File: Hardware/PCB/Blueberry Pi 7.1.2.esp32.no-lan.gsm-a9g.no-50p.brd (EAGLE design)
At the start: 80.7 x 60.9 mm, 231 parts, among them J2 AUDIO_JACK_SMD, J3 USB-A-FEMALE, Q1 24Mhz, Q2 32kHz, U1 MICROSIM, U2 W25Q32FV, U3 AP3031KTR-G1, U4 ESP-WROOM-32, U5 W25Q40BVSS, X1 FH12-50S-0.5SH, X2 53047-02

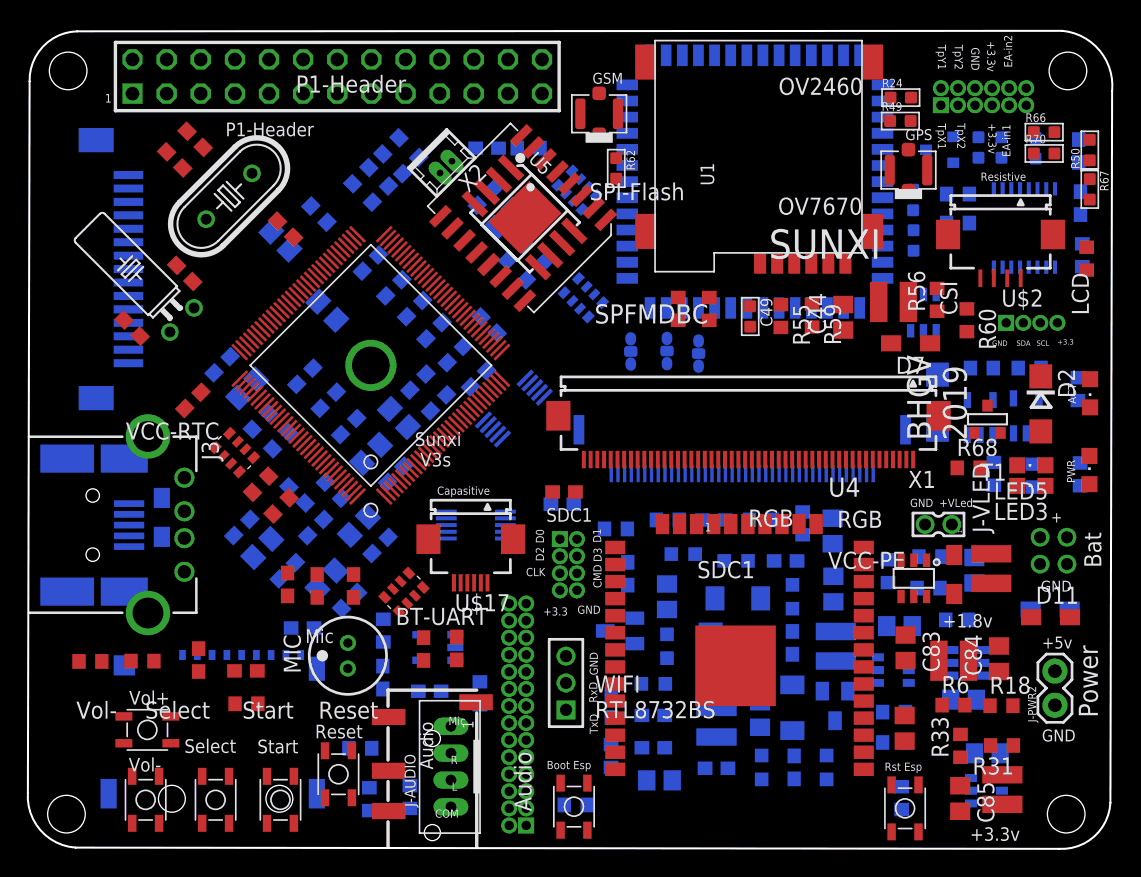
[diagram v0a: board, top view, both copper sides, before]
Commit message: better connected A9G module. added 'no-50pin lcd' schematic easier for router and with headers for the rest of A9G pins
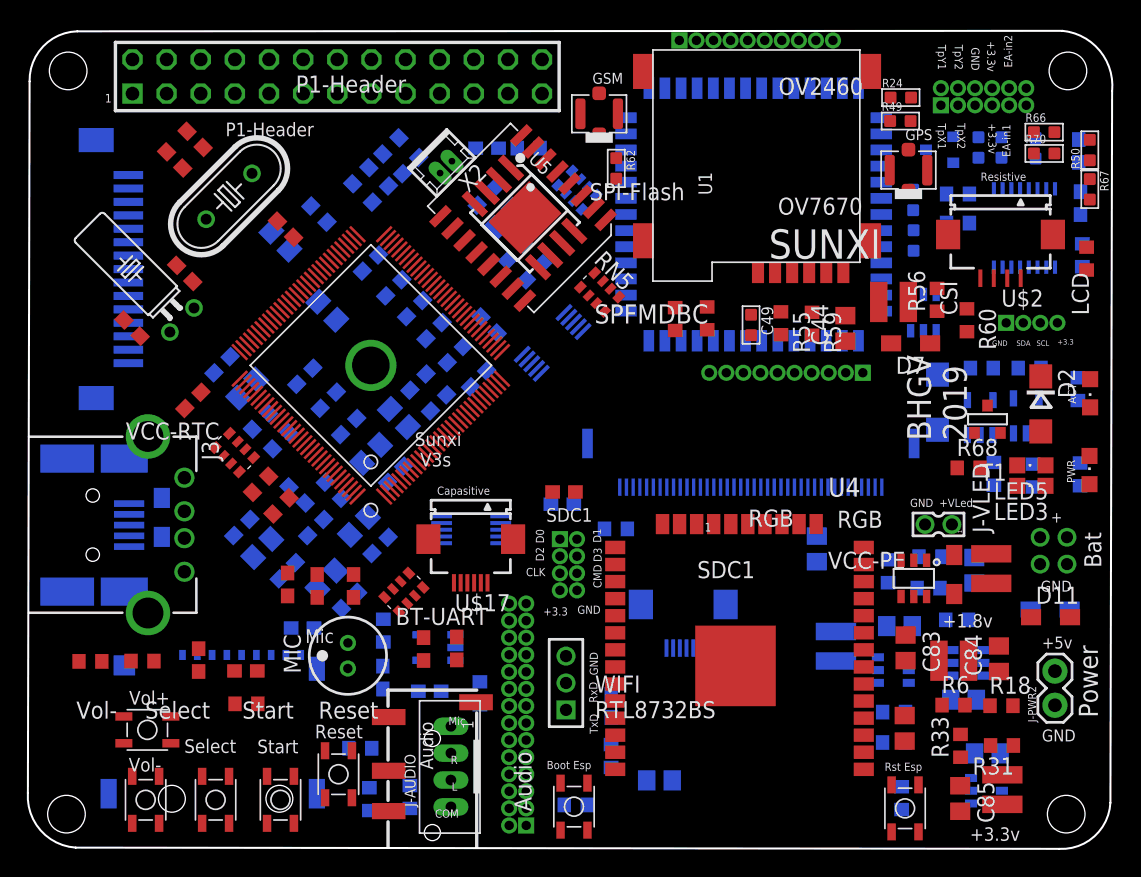
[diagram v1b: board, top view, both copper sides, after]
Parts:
- removed C31, C6: 22uF/6.3V, rcl:C0805
- removed C32, C33, C35, C4, C40, C41, C42, C43: 100nF, rcl:C0603
- removed C5: 10uF/16V, rcl:C0805
- removed D3, D4: BAT54S, semicon-smd-ipc:SOT23C(BAT54S)
- removed D5: 1N5819/SS14, gogo:MINI-MELF
- removed JMP1, JMP2, JMP3: 0R-JUMPC, jump-0r-smd:C0R-JMP
- removed L3: 47µH, induct-CD:CD32
- removed R10, R7: 10k, rcl:R0603
- removed R19, R40, R42: 51k/1%, rcl:R0603_5MIL
- removed R34, R37, R41: 1k/1%, rcl:R0603_5MIL
- removed R35: 20k, rcl:R0603_5MIL
- removed R9: 30k, rcl:R0603
- removed U3: AP3031KTR-G1, OLIMEX_IC:SOT23-6
- removed X1: FH12-50S-0.5SH, con-hirose:FH12-50S-0.5SH
- removed Z1: BZV55C6V8, gogo:MINI-MELF
- removed Z2: BZV55C16, gogo:MINI-MELF
- added DBG-COM1, DBG-COM2: HDR-1.27MM-110, headers-1.27:HDR-1.27MM-1*10
- added U$21: FH12-06S-0.5S, con-hirose:FH12-6S-0.5SH
- moved U$19 5.68 mm to (50.5, 38.1), turned to 135 degrees
- moved U6 2.45 mm to (65.4, 47.6)
- moved C73 1.78 mm to (70.1, 22.7)
- moved RN5 1.28 mm to (54.0, 41.8), flipped to the top, turned to 315 degrees
- moved J-LCD-FFC 1.20 mm to (65.2, 30.5)
- moved C44 0.84 mm to (72.3, 39.1)
- moved R44 0.79 mm to (59.6, 39.8)
- moved R45 0.72 mm to (62.0, 39.9)
- moved U1 0.72 mm to (73.3, 44.1)
- moved C49 0.64 mm to (65.2, 39.4)
- moved R59 0.60 mm to (69.8, 39.5)
- moved R55 0.54 mm to (67.5, 39.5)
- moved U$24 0.49 mm to (44.4, 24.2)
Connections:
- removed net -7V: C43.1, R41.1, R42.2, X1.42, Z1.2
- removed net 10.4V: C32.1, C5.1, D4.1, D5.1, R19.2, R35.2, U3.5, X1.43
- removed net 16V: C40.1, R37.1, R40.2, R9.1, X1.41, Z2.1
- removed net L/R: JMP1.2, X1.39
- removed net N$123: C33.1, C41.2, D5.2, L3.P$2, U3.1
- removed net N$126: R19.1, R34.1, U3.3
- removed net N$17: C4.1, R10.2, X1.44
- removed net N$24: JMP3.2, X1.47
- removed net N$25: C33.2, D4.3
- removed net N$27: C35.1, D4.2, R37.2
- removed net N$34: C42.1, D3.1, R41.2
- removed net N$37: C41.1, D3.3
- removed net U/D: JMP2.2, X1.40
- removed net VCOM: R7.1, R9.2, X1.46, X1.6
- new net A9G_HST_RXD: DBG-COM1.P$1, U6.38
- new net A9G_HST_TXD: DBG-COM1.P$2, U6.37
- new net A9G_IO26: DBG-COM2.P$7, U6.25
- new net A9G_IO27: DBG-COM2.P$8, U6.26
- new net A9G_IO28: DBG-COM2.P$9, U6.30
- new net A9G_IO29: DBG-COM1.P$8, U6.24
- new net A9G_IO30: DBG-COM2.P$10, U6.31
- new net A9G_LCD_CS: DBG-COM1.P$7, U6.19
- new net A9G_LCD_DIO: DBG-COM1.P$5, U6.21
- new net A9G_LCD_RST: DBG-COM1.P$6, U6.20
- new net A9G_LCD_SCK: DBG-COM1.P$3, U6.23
- new net A9G_LCD_SDC: DBG-COM1.P$4, U6.22
- new net A9G_SD_CLK: DBG-COM2.P$6, U6.8
- new net A9G_SD_CMD: DBG-COM2.P$5, U6.7
- new net A9G_SD_D0: DBG-COM2.P$4, U6.6
- new net A9G_SD_D1: DBG-COM2.P$3, U6.5
- new net A9G_SD_D2: DBG-COM2.P$2, U6.4
- new net A9G_SD_D3: DBG-COM2.P$1, U6.3
- new net N$85: J-LCD-FFC.1
- net !RESET: now also U$21.6
- net +3V3: now also DBG-COM1.P$9, U$21.5; no longer JMP1.3, JMP2.3, JMP3.1, R10.1, X1.7, X1.8
- net +5V: no longer C31.2, C6.2, L3.P$1, U3.4, U3.6
- net CSI_D0/LCD_D2: no longer X1.17
- net CSI_D1/LCD_D3: no longer X1.16
- net CSI_D10/LCD_D14: no longer X1.21
- net CSI_D11/LCD_D15: no longer X1.20
- net CSI_D12/LCD_D18: no longer X1.33
- net CSI_D2/LCD_D4: no longer X1.15
- net CSI_D3/LCD_D5: no longer X1.14
- net CSI_D4/LCD_D6: no longer X1.13
- net CSI_D5/LCD_D7: no longer X1.12
- net CSI_D6/LCD_D10: no longer X1.25
- net CSI_D7/LCD_D11: no longer X1.24
- net CSI_D8/LCD_D12: no longer X1.23
- net CSI_D9/LCD_D13: no longer X1.22
- net CSI_HSYNC/LCD_HSYNC: no longer X1.11
- net CSI_MCLK/LCD_DE: no longer X1.9
- net CSI_PCLK/LCD_CLK: no longer X1.37
- net CSI_VSYNC/LCD_VSYNC: no longer X1.10
- net GND: now also DBG-COM1.P$10, U$21.4; no longer C31.1, C32.2, C35.2, C4.2, C40.2, C42.2, C43.2, C5.2, C6.1, D3.2, JMP1.1, JMP2.1, JMP3.3, R34.2, R35.1, R40.1, R42.1, R7.2, U3.2, X1.18, X1.19, X1.26, X1.27, X1.34, X1.35, X1.36, X1.38, X1.48, X1.5, Z1.1, Z2.2
- net HP_L: no longer J-AUDIO.P3
- net HP_L_O: now also J-AUDIO.P3
- net HP_R: no longer J-AUDIO.P2
- net HP_R_O: now also J-AUDIO.P2
- net I2C1/SCL: now also U$21.1
- net I2C1/SDA: now also U$21.2
- net LCD_D19: no longer X1.32
- net LCD_D20: no longer X1.31
- net LCD_D21: no longer X1.30
- net LCD_D22: no longer X1.29
- net LCD_D23: no longer X1.28
- net PB3: now also U$21.3
- net VLED+: no longer X1.1, X1.2
- net VLED-: no longer J-LCD-FFC.1, X1.3, X1.4
